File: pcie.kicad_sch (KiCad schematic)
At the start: 21 parts, among them U15 XC7K160T-FFG676

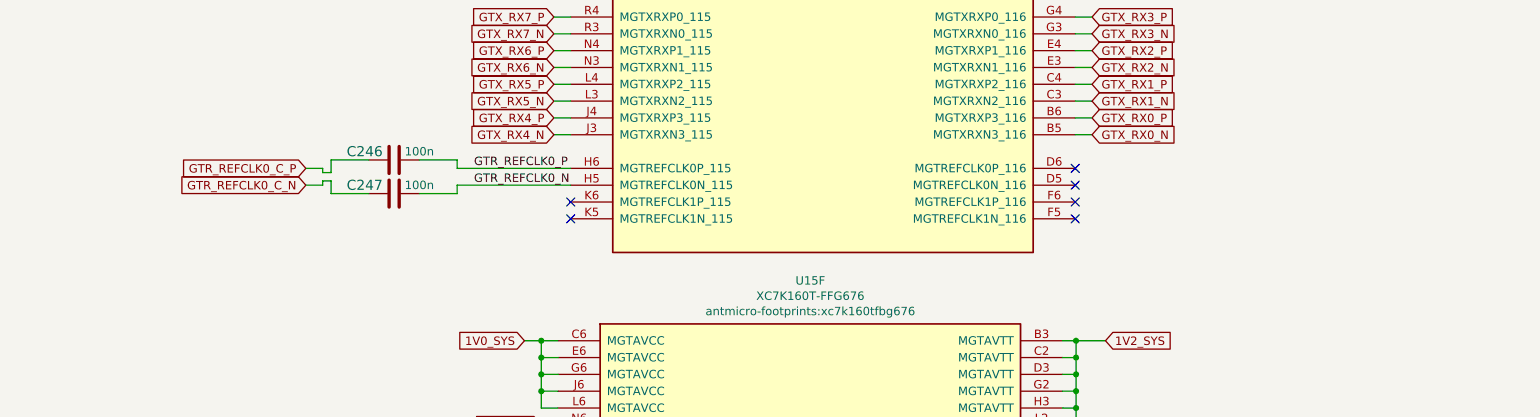
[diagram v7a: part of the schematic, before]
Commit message: Optimize BOM, add all bank 115 and 116 REFCLK's to FMC connector
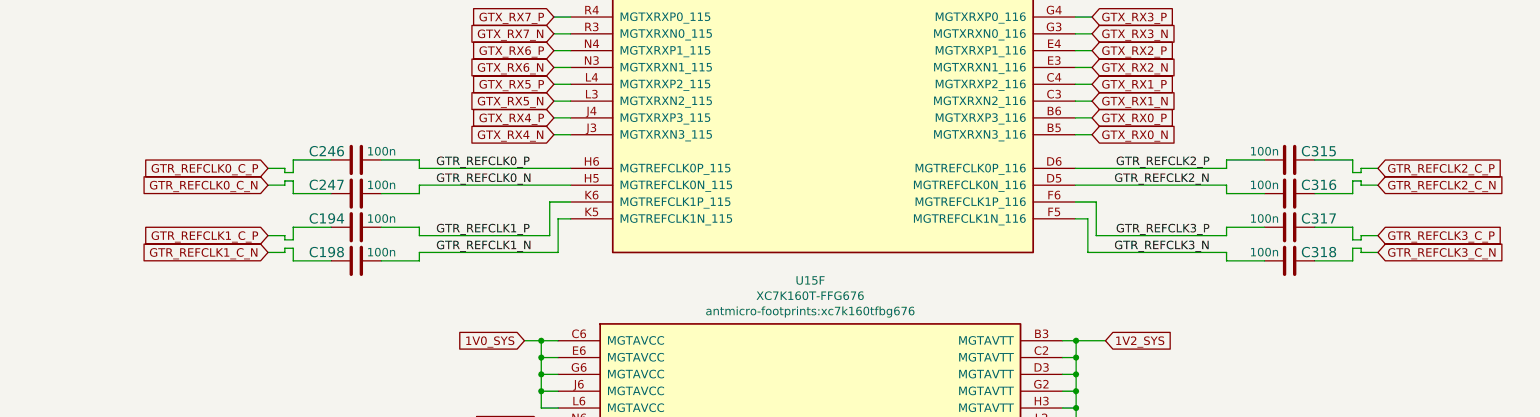
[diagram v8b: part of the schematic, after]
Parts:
- added C194, C198, C315, C316, C317, C318: C_100n_0402, antmicro-footprints:0402-cap, symbol antmicroCapacitors0402:C_100n_0402
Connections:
- net GTR_REFCLK2_N: now reaches U15.D5 (MGTREFCLK0N_116)
- net GTR_REFCLK2_N: now also C316.2
- net GTR_REFCLK2_P: now reaches U15.D6 (MGTREFCLK0P_116)
- net GTR_REFCLK2_P: now also C315.2
- net GTR_REFCLK3_N: now reaches U15.F5 (MGTREFCLK1N_116)
- net GTR_REFCLK3_N: now also C318.2
- net GTR_REFCLK3_P: now reaches U15.F6 (MGTREFCLK1P_116)
- net GTR_REFCLK3_P: now also C317.2
- net GTR_REFCLK1_N: now reaches U15.K5 (MGTREFCLK1N_115)
- net GTR_REFCLK1_N: now also C198.2
- net GTR_REFCLK1_P: now reaches U15.K6 (MGTREFCLK1P_115)
- net GTR_REFCLK1_P: now also C194.2
- new net GTR_REFCLK1_C_N: C198.1
- new net GTR_REFCLK1_C_P: C194.1
- new net GTR_REFCLK2_C_N: C316.1
- new net GTR_REFCLK2_C_P: C315.1
- new net GTR_REFCLK3_C_N: C318.1
- new net GTR_REFCLK3_C_P: C317.1
- no-connect marks 6 -> 0
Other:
- moved on the sheet: C246, C247
